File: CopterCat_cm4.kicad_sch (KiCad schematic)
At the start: 0 parts

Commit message: плата практически готова
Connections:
- no-connect marks 0 -> 6
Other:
- sheet Connectors ports: added PWR_IN_CONN, PWR_IN_JST, VBUS; removed VBUS_SENSE
- sheet Power ports: added 3V3_GROUP1, 3V3_GROUP2, 5V_GROUP1, 5V_GROUP2, 5V_GROUP3, PWR_IN_CONN, PWR_IN_JST, USB_SWITCH, VBUS; removed none
- sheet USB_HUB ports: added USB_SWITCH, VBUS_SENSE; removed none
- note added: "Not used"

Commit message: тестирование
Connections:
- no-connect marks 6 -> 0
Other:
- sheet STM32 ports: added none; removed STM_I2C2{I2C}, STM_I2C3{I2C}, STM_SPI4{SPI}, STM_SPI6{SPI NRESET}, STM_UART4{UART}, STM_UART8{UART}
- note removed: "Not used"
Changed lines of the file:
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@@
   (bus_alias "I2C" (members "SCL" "SDA" "DRDY[1..5]"))
   (bus_alias "UART" (members "TX" "RX" "RTS" "CTS"))
+  (bus_alias "CSI" (members "D_P[0..3]" "D_N[0..3]" "C_P" "C_N"))
   (bus_alias "USB" (members "DP" "DN" "ID" "VBUS"))
   (bus_alias "SPI" (members "SCK" "MISO" "MOSI" "CS[1..5]" "DRDY[1..5]"))
-  (bus_alias "CSI" (members "D_P[0..3]" "D_N[0..3]" "C_P" "C_N"))
   (junction (at 147.32 90.17) (diameter 0) (color 0 0 0 0)
   )
   (junction (at 195.58 90.17) (diameter 0) (color 0 0 0 0)
   )
-  (no_connect (at 87.63 63.5))
-  (no_connect (at 87.63 66.04))
-  (no_connect (at 87.63 55.88))
-  (no_connect (at 87.63 58.42))
-  (no_connect (at 87.63 60.96))
-  (no_connect (at 87.63 68.58))
   (wire (pts (xy 195.58 74.93) (xy 200.66 74.93))
     (stroke (width 0) (type default) (color 0 0 0 0))
@@
     (stroke (width 0) (type default) (color 0 0 0 0))
   )
-  (polyline (pts (xy 114.3 69.85) (xy 114.3 50.8))
-    (stroke (width 0) (type default) (color 0 0 0 0))
-  )
   (bus (pts (xy 144.78 104.14) (xy 144.78 54.61))
     (stroke (width 0) (type default) (color 0 0 0 0))
@@
     (stroke (width 0) (type default) (color 0 0 0 0))
   )
-  (bus (pts (xy 87.63 63.5) (xy 90.17 63.5))
-    (stroke (width 0) (type default) (color 0 0 0 0))
-  )
   (wire (pts (xy 194.31 72.39) (xy 200.66 72.39))
     (stroke (width 0) (type default) (color 0 0 0 0))
@@
     (stroke (width 0) (type default) (color 0 0 0 0))
   )
-  (polyline (pts (xy 114.3 50.8) (xy 90.17 50.8))
-    (stroke (width 0) (type default) (color 0 0 0 0))
-  )
   (wire (pts (xy 147.32 90.17) (xy 151.13 90.17))
     (stroke (width 0) (type default) (color 0 0 0 0))
@@
     (stroke (width 0) (type default) (color 0 0 0 0))
   )
-  (polyline (pts (xy 90.17 69.85) (xy 114.3 69.85))
-    (stroke (width 0) (type default) (color 0 0 0 0))
-  )
   (bus (pts (xy 248.92 77.47) (xy 248.92 92.71))
     (stroke (width 0) (type default) (color 0 0 0 0))
   )
-  (bus (pts (xy 87.63 58.42) (xy 90.17 58.42))
-    (stroke (width 0) (type default) (color 0 0 0 0))
-  )
   (wire (pts (xy 186.69 63.5) (xy 200.66 63.5))
     (stroke (width 0) (type default) (color 0 0 0 0))
   )
-  (bus (pts (xy 87.63 60.96) (xy 90.17 60.96))
-    (stroke (width 0) (type default) (color 0 0 0 0))
-  )
   (wire (pts (xy 148.59 110.49) (xy 148.59 104.14))
     (stroke (width 0) (type default) (color 0 0 0 0))
@@
     (stroke (width 0) (type default) (color 0 0 0 0))
   )
-  (bus (pts (xy 87.63 68.58) (xy 90.17 68.58))
-    (stroke (width 0) (type default) (color 0 0 0 0))
-  )
   (wire (pts (xy 236.22 77.47) (xy 236.22 92.71))
     (stroke (width 0) (type default) (color 0 0 0 0))
   )
-  (bus (pts (xy 87.63 55.88) (xy 90.17 55.88))
-    (stroke (width 0) (type default) (color 0 0 0 0))
-  )
   (bus (pts (xy 73.66 87.63) (xy 81.28 87.63))
     (stroke (width 0) (type default) (color 0 0 0 0))
@@
   )
   (wire (pts (xy 147.32 107.95) (xy 147.32 90.17))
-    (stroke (width 0) (type default) (color 0 0 0 0))
-  )
-  (bus (pts (xy 87.63 66.04) (xy 90.17 66.04))
     (stroke (width 0) (type default) (color 0 0 0 0))
   )
@@
     )
   )
-  (text "Not used" (at 90.17 53.34 0)
-    (effects (font (size 1.27 1.27) (thickness 0.254) bold) (justify left bottom))
-  )
   (sheet (at 90.17 27.94) (size 49.53 59.69) (fields_autoplaced)
     (stroke (width 0) (type solid) (color 0 0 0 0))
@@
     (pin "STM_DEBUG{DEBUG}" input (at 139.7 38.1 0)
       (effects (font (size 1.27 1.27)) (justify right))
-    )
-    (pin "STM_UART4{UART}" input (at 90.17 66.04 180)
-      (effects (font (size 1.27 1.27)) (justify left))
-    )
-    (pin "STM_UART8{UART}" input (at 90.17 68.58 180)
-      (effects (font (size 1.27 1.27)) (justify left))
-    )
-    (pin "STM_SPI6{SPI NRESET}" input (at 90.17 63.5 180)
-      (effects (font (size 1.27 1.27)) (justify left))
-    )
-    (pin "STM_SPI4{SPI}" input (at 90.17 60.96 180)
-      (effects (font (size 1.27 1.27)) (justify left))
-    )
-    (pin "STM_I2C2{I2C}" input (at 90.17 55.88 180)
-      (effects (font (size 1.27 1.27)) (justify left))
-    )
-    (pin "STM_I2C3{I2C}" input (at 90.17 58.42 180)
-      (effects (font (size 1.27 1.27)) (justify left))
     )
     (pin "STM_RC{RX PPM PWR}" input (at 139.7 45.72 0)
@@
       (reference "#PWR0140") (unit 1) (value "GND") (footprint "")
     )
+    (path "/00000000-0000-0000-0000-000061c29261/a1e6e2c4-397e-4467-9a6c-eb9cdfe26fd1"
+      (reference "#PWR0141") (unit 1) (value "GND") (footprint "")
+    )
     (path "/00000000-0000-0000-0000-000061c29261/00000000-0000-0000-0000-000061d36c7a"
       (reference "#PWR0142") (unit 1) (value "GND") (footprint "")
@@
       (reference "#PWR0172") (unit 1) (value "GND") (footprint "")
     )
-    (path "/00000000-0000-0000-0000-000061c29261/a1e6e2c4-397e-4467-9a6c-eb9cdfe26fd1"
-      (reference "#PWR?") (unit 1) (value "GND") (footprint "")
-    )
     (path "/00000000-0000-0000-0000-000061c250a4/1a28e523-8149-4b77-b61b-12daef28fcac"
       (reference "ANT1") (unit 1) (value "ANT016008LCS2442MA2") (footprint "ANT016008LCS2442MA2:ANT_ANT016008LCS2442MA2")
@@
       (reference "D7") (unit 1) (value "1N5819WS") (footprint "Diode_SMD:D_SOD-323")
     )
-    (path "/00000000-0000-0000-0000-000061c250a4/00000000-0000-0000-0000-000061c954c1"
-      (reference "F2") (unit 1) (value "BLM15BC241SN1D") (footprint "Fuse:Fuse_0402_1005Metric")
-    )
-    (path "/00000000-0000-0000-0000-000061c250a4/00000000-0000-0000-0000-000061ccf994"
-      (reference "F3") (unit 1) (value "BLM15BC241SN1D") (footprint "Fuse:Fuse_0402_1005Metric")
-    )
     (path "/00000000-0000-0000-0000-000061c29261/eb6a987e-b044-454b-b090-77b23595518e"
-      (reference "GND") (unit 1) (value "Conn_01x01_Male") (footprint "TestPoint:TestPoint_Pad_D2.0mm")
+      (reference "GND1") (unit 1) (value "Conn_01x01_Male") (footprint "TestPoint:TestPoint_Pad_D1.5mm")
     )
     (path "/00000000-0000-0000-0000-000061c29261/00000000-0000-0000-0000-000061c3eb84"
@@
     )
     (path "/00000000-0000-0000-0000-000061c29261/82a33a3d-e58b-4485-82cc-38155ff14a84"
-      (reference "LED") (unit 1) (value "Conn_01x01_Male") (footprint "TestPoint:TestPoint_Pad_D2.0mm")
+      (reference "LED1") (unit 1) (value "Conn_01x01_Male") (footprint "TestPoint:TestPoint_Pad_D1.5mm")
     )
     (path "/00000000-0000-0000-0000-000061c29261/00000000-0000-0000-0000-000061c4e148"

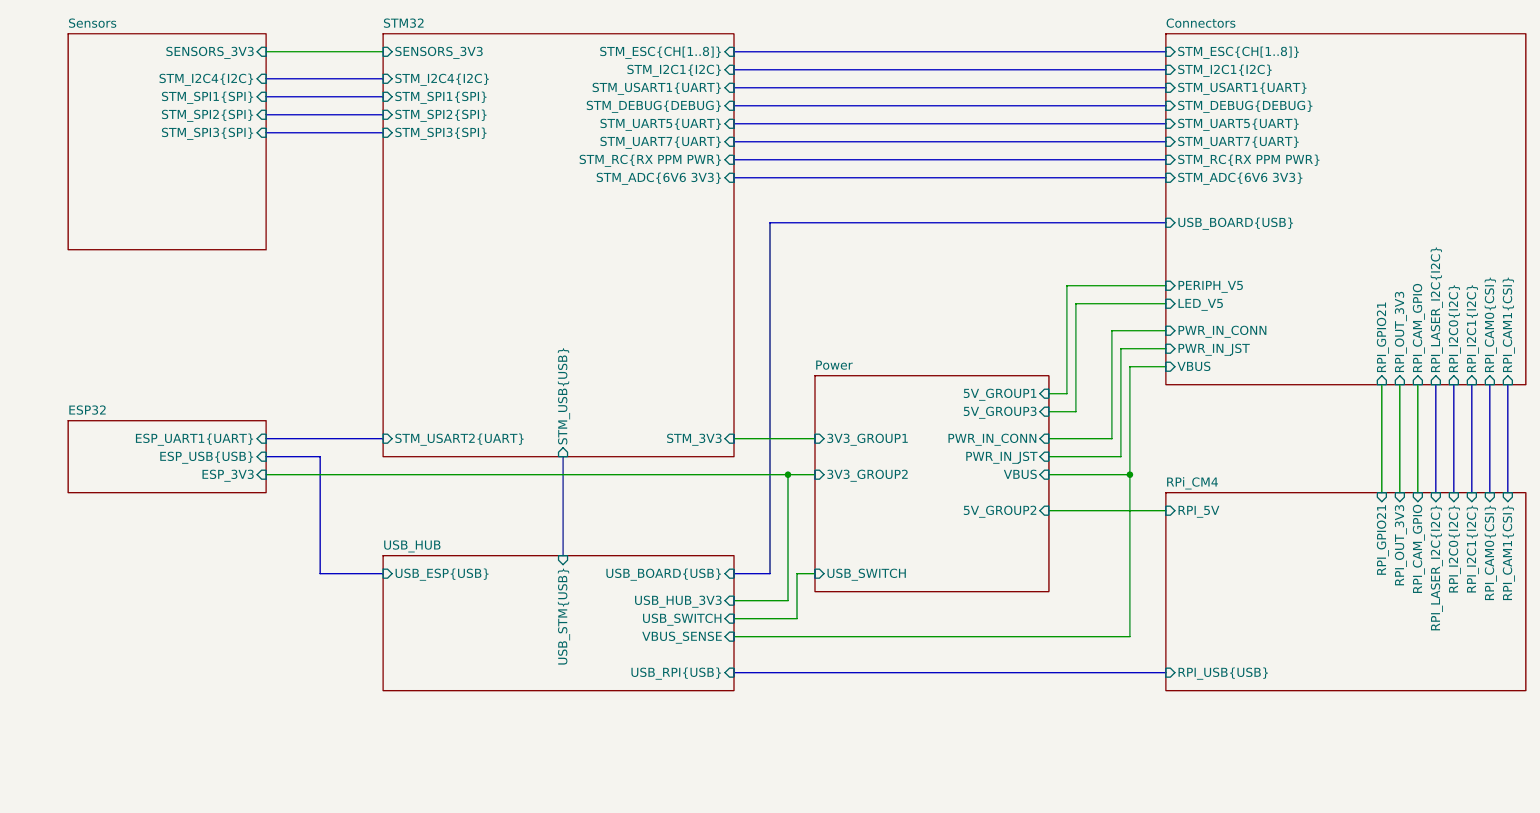
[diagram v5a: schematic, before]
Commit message: Adding esp32 gpio pins
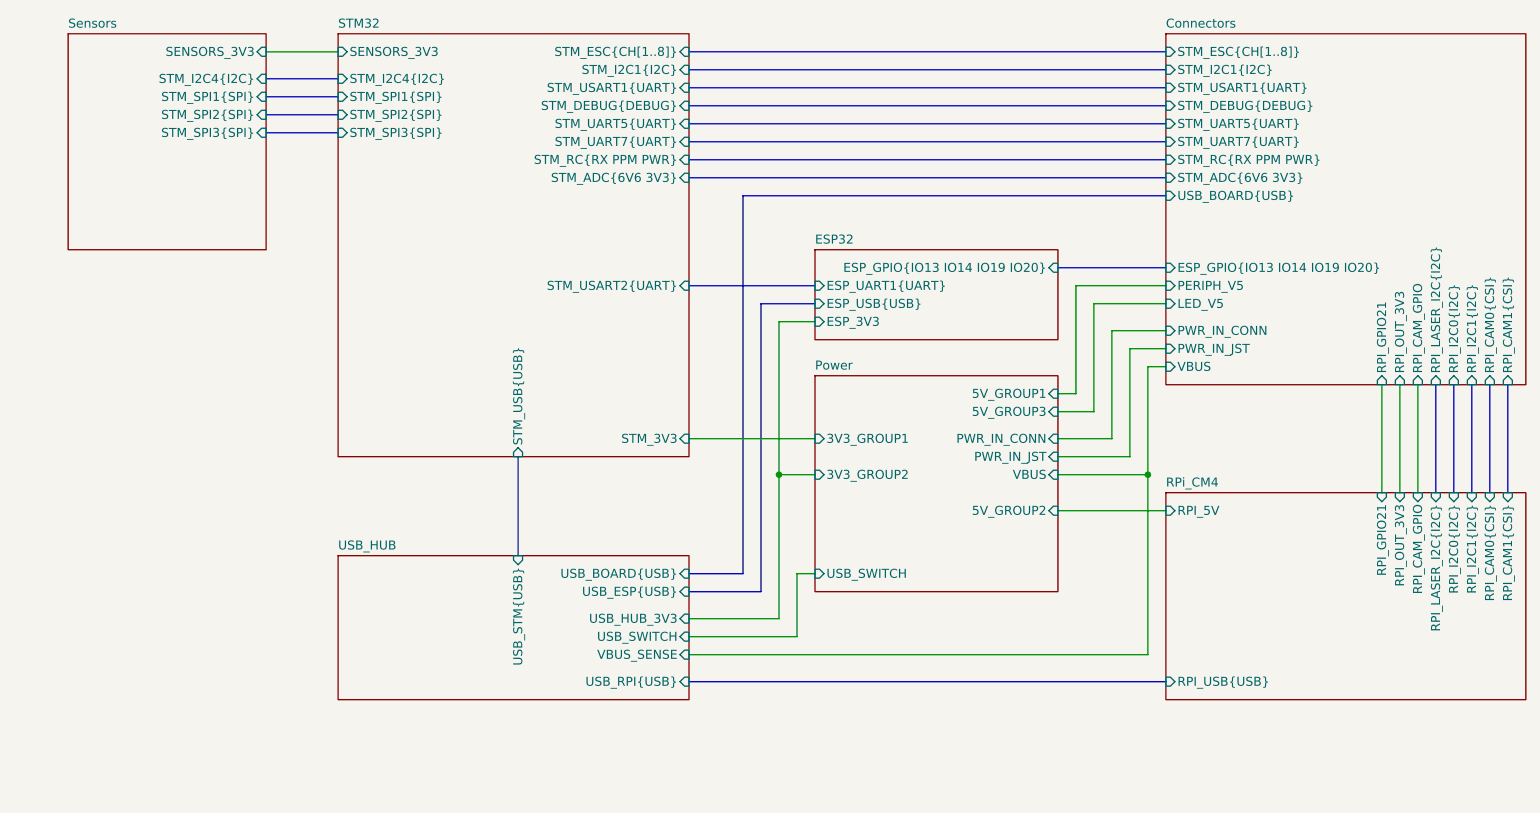
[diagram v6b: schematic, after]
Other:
- sheet Connectors ports: added ESP_GPIO{IO13 IO14 IO19 IO20}; removed none
- sheet ESP32 ports: added ESP_GPIO{IO13 IO14 IO19 IO20}; removed none
